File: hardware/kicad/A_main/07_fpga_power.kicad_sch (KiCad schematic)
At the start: 41 parts, among them J10 JTAG 2x3, SW1 PROG, U10 LFE5U-25F-7BG256I, U11 W25Q128JVSIQ

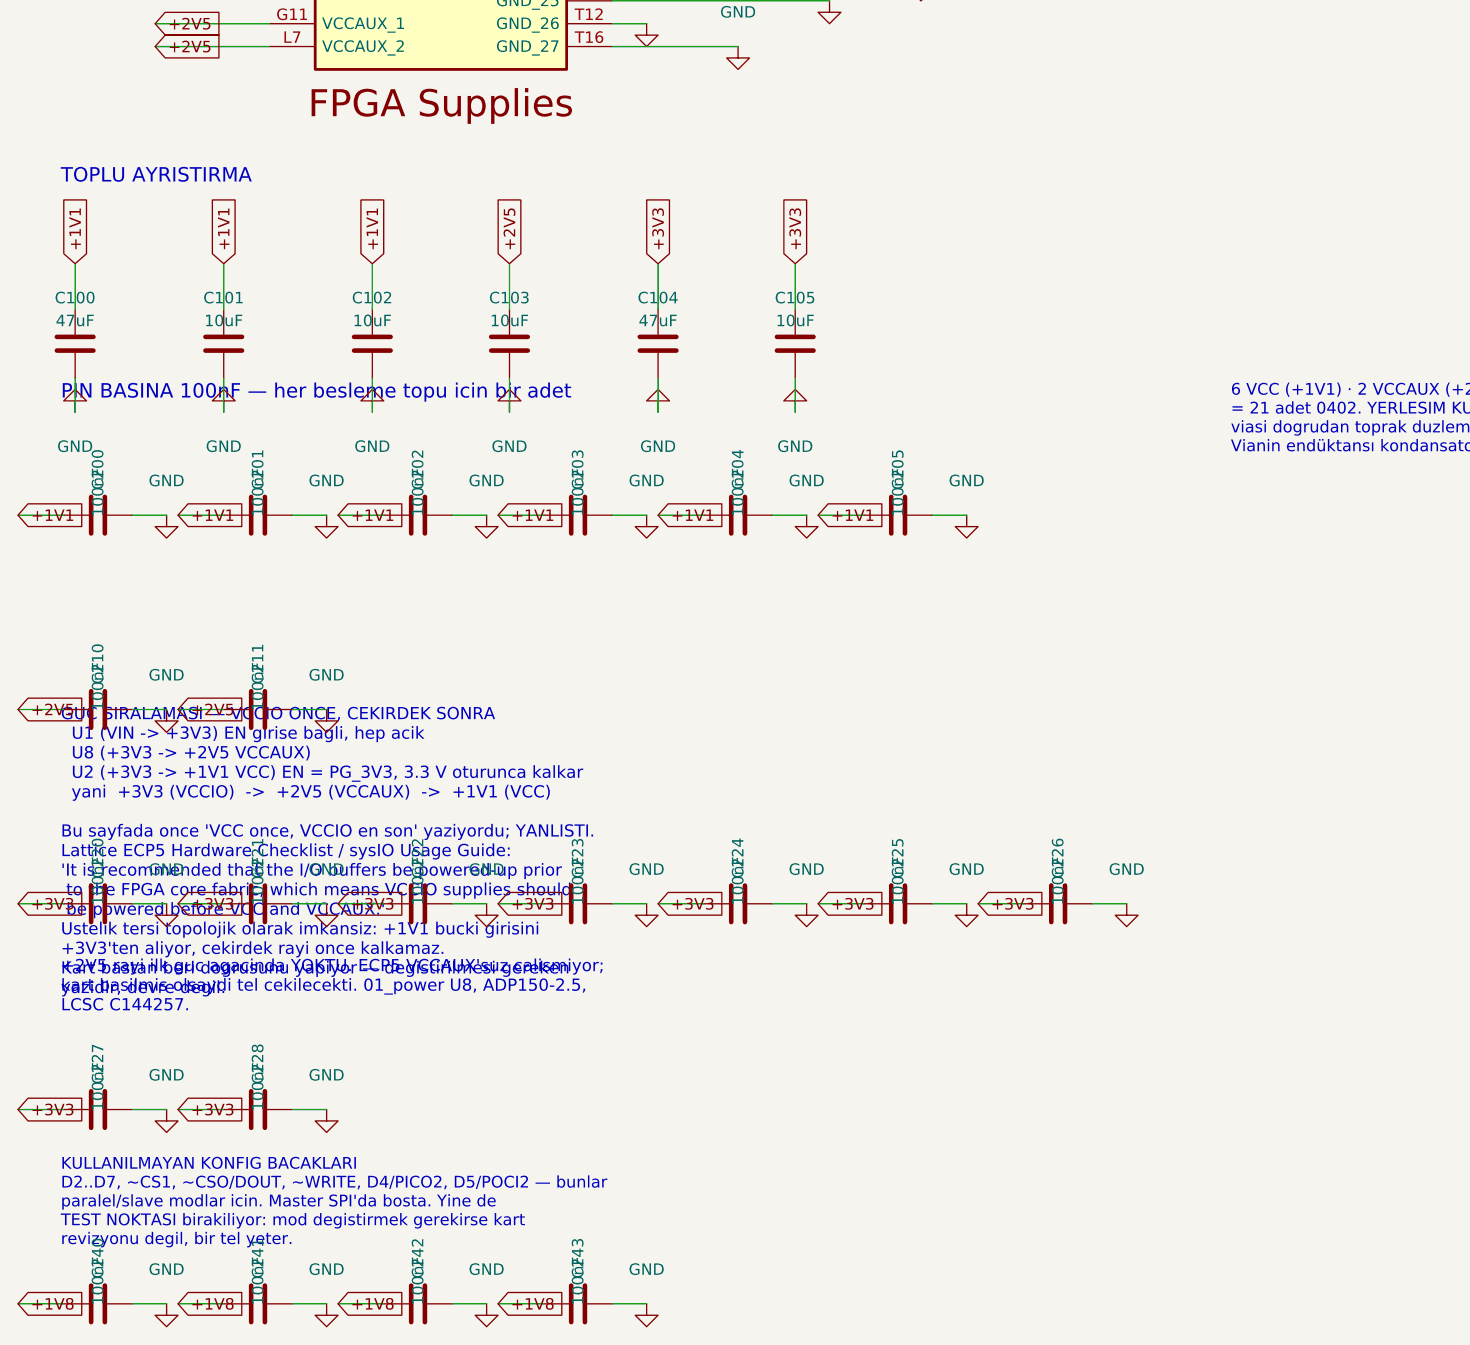
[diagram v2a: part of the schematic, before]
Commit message: Add bulk capacitors to the 1.8 V rails and measure the supply network
Counting decoupling capacitors is not enough. The existing check asks
whether each supply pin has a capacitor. That is necessary but not
sufficient. What matters is the impedance that the chip sees on the
rail, against frequency. No connectivity check can see this: the
schematic is correct, the netlist is correct, the DRC is clean, and
the rail still rings.

The +1V8 rail and the +1V8_D rail had no bulk capacitor. The largest
part was 1 uF. The regulator loop holds the impedance low to about
100 kHz. The ceramics hold it above about 1 MHz. Between them there
was nothing. The peak impedance on +1V8 was 994 mohm against a target
of 360 mohm.

This result does not depend on an assumption. A rail with no bulk
capacitor is a gap whatever transient current you assume.

The +1V1 core rail was also marginal: 228 mohm against 183 mohm. In
the upper band the impedance comes from the mounting inductance
divided by the number of capacitors, not from the value. So the
number changed, not the value.

Added: 22 uF and 10 uF on +1V8, 10 uF on +1V8_D. The 100 nF count
went from 6 to 14 on +1V1 and from 4 to 8 on +1V8. All rails now pass
with margin.

Three errors in the tool were corrected. Each one would have reversed
the answer:

The sweep went to 1 GHz, and every rail failed with its peak at
987 MHz, the top of the sweep. That was not an anti-resonance. The
model has no die capacitance, so the impedance rose without limit.
The board is responsible to about 200 MHz.

The regulator was a fixed 100 nH inductor, and this made a sharp
false resonance at 0.4 MHz. A switching regulator holds its output
impedance low up to its own crossover. Above that the bulk capacitors
dominate, and they were already counted. The same thing was counted
twice.

The transient current of the ECP5 core was 1.5 A, and the tool asked
for 37 capacitors. That number came from the assumption. The
LFE5U-25F is a small FPGA and its core curren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
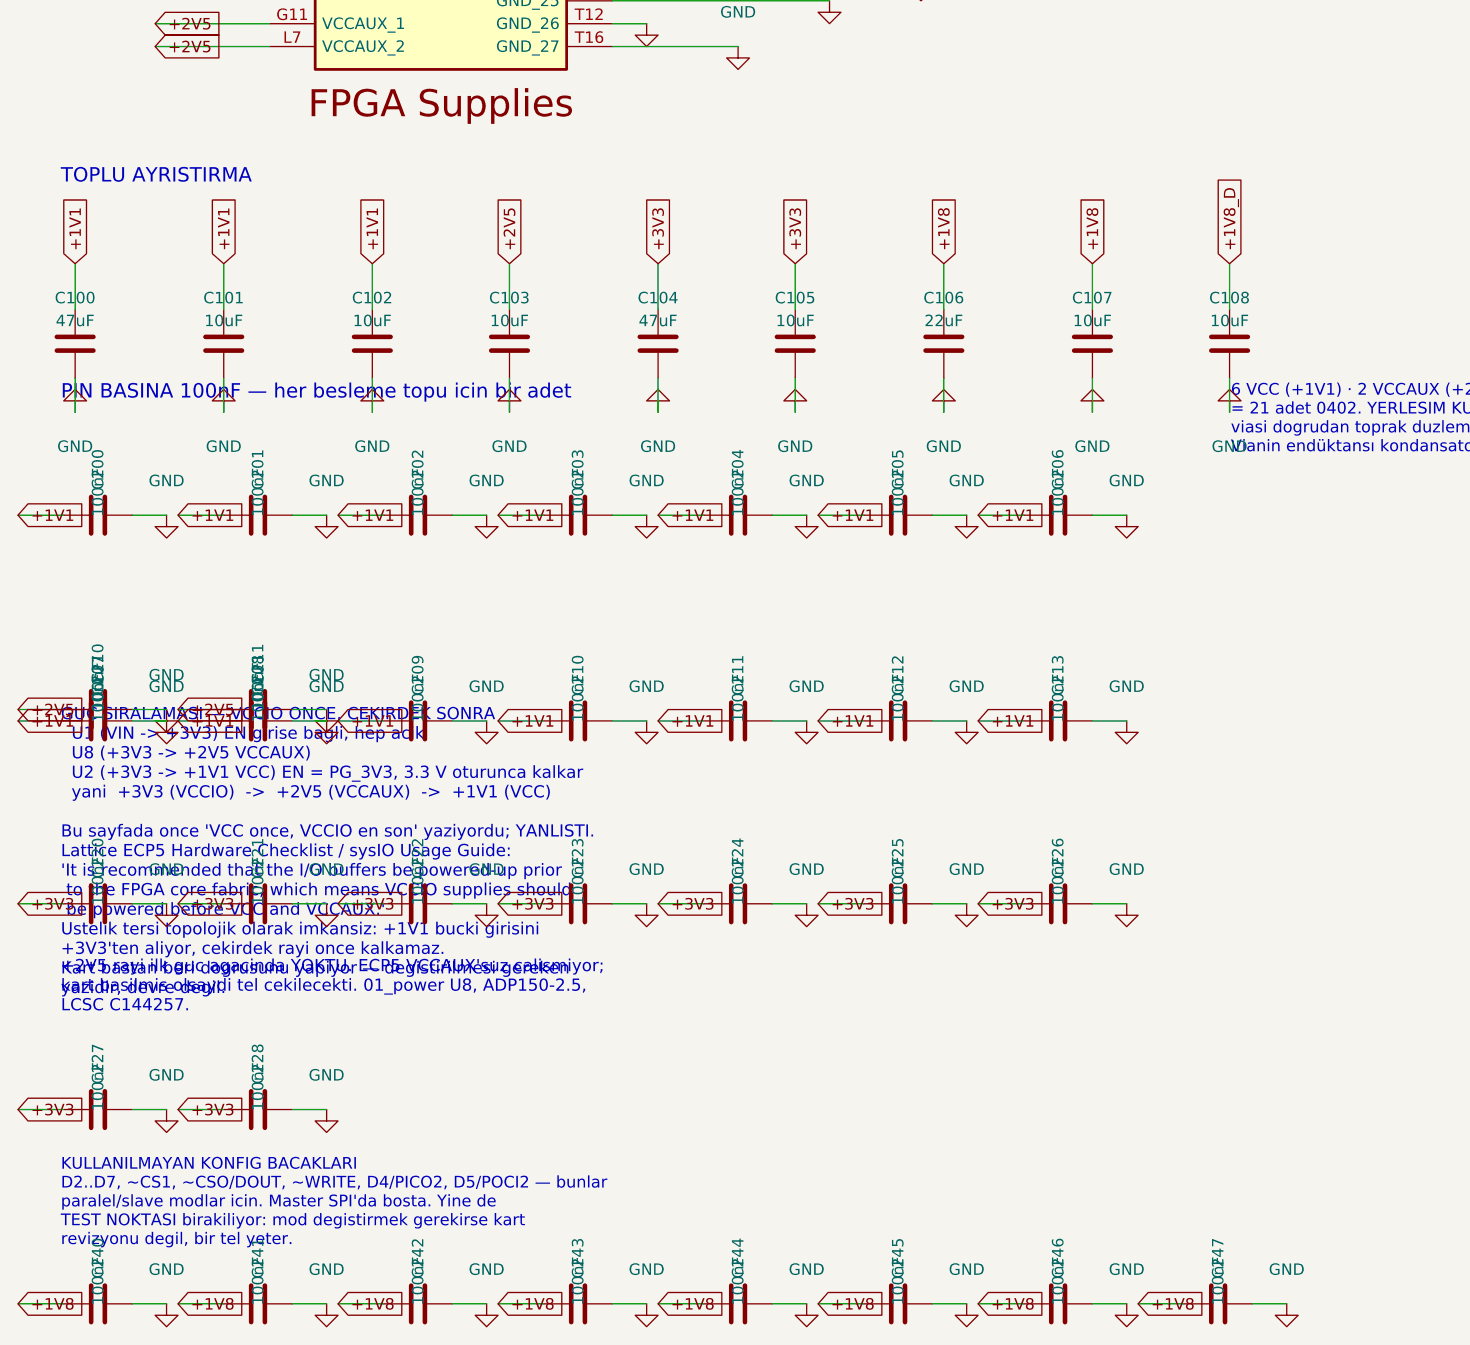
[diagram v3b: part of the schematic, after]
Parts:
- removed C210, C211: 100nF, Capacitor_SMD:C_0402_1005Metric, symbol Device:C
- added C106: 22uF, Capacitor_SMD:C_1206_3216Metric, symbol Device:C
- added C107, C108: 10uF, Capacitor_SMD:C_0603_1608Metric, symbol Device:C
- added C206, C207, C208, C209, C210 (x2), C211 (x2), C212, C213, C244, C245, C246, C247: 100nF, Capacitor_SMD:C_0402_1005Metric, symbol Device:C
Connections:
- net +1V1: now also C206.1, C207.1, C208.1, C209.1, C210.1, C211.1, C212.1, C213.1
- net +1V8: now also C106.1, C107.1, C244.1, C245.1, C246.1, C247.1
- net +2V5: now also C210.1, C211.1
- net GND: now also C106.2, C107.2, C108.2, C206.2, C207.2, C208.2, C209.2, C210.2, C210.2, C211.2, C211.2, C212.2, C213.2, C244.2, C245.2, C246.2, C247.2
- new net +1V8_D: C108.1
